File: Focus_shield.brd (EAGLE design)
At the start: 60.5 x 54.4 mm, 61 parts, among them U1 ARDUINO_SHIELDNOHOLES

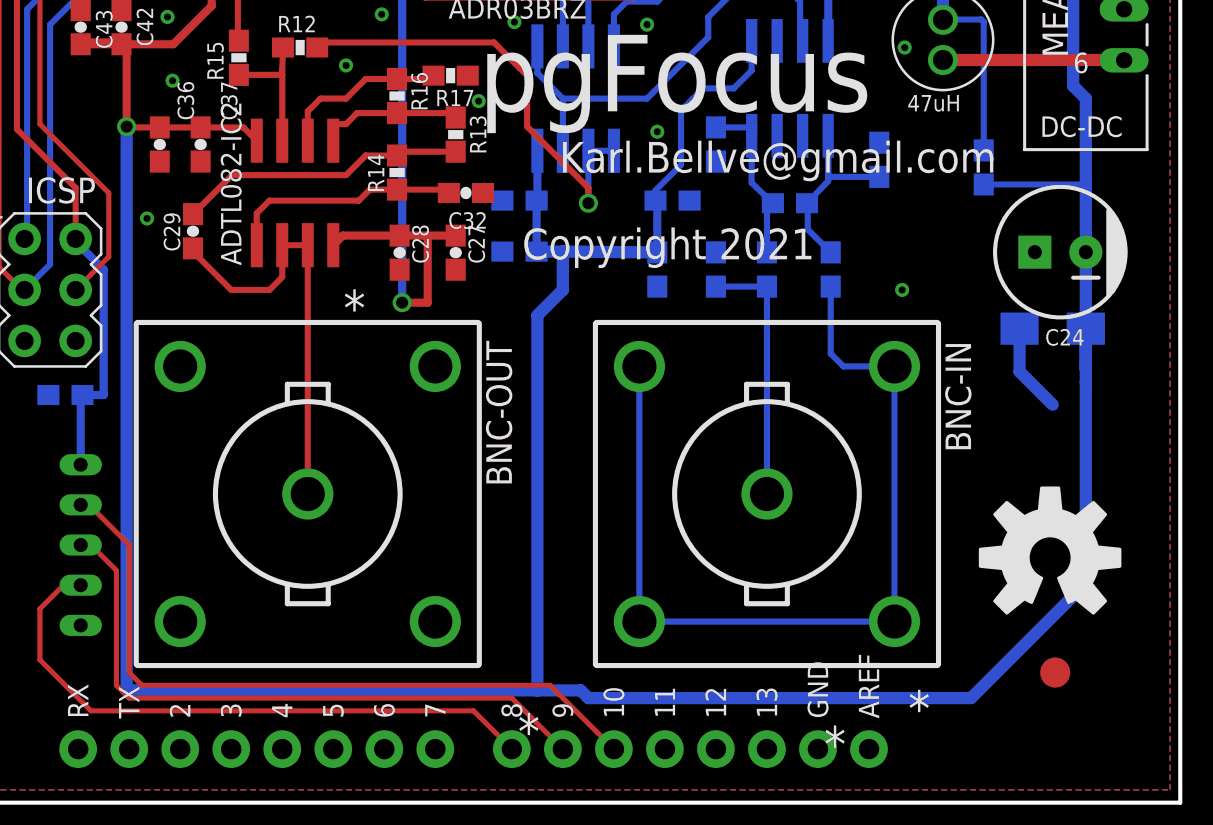
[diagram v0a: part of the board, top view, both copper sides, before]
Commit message: switch type of BNC users, and added a link to BOM spreadsheet
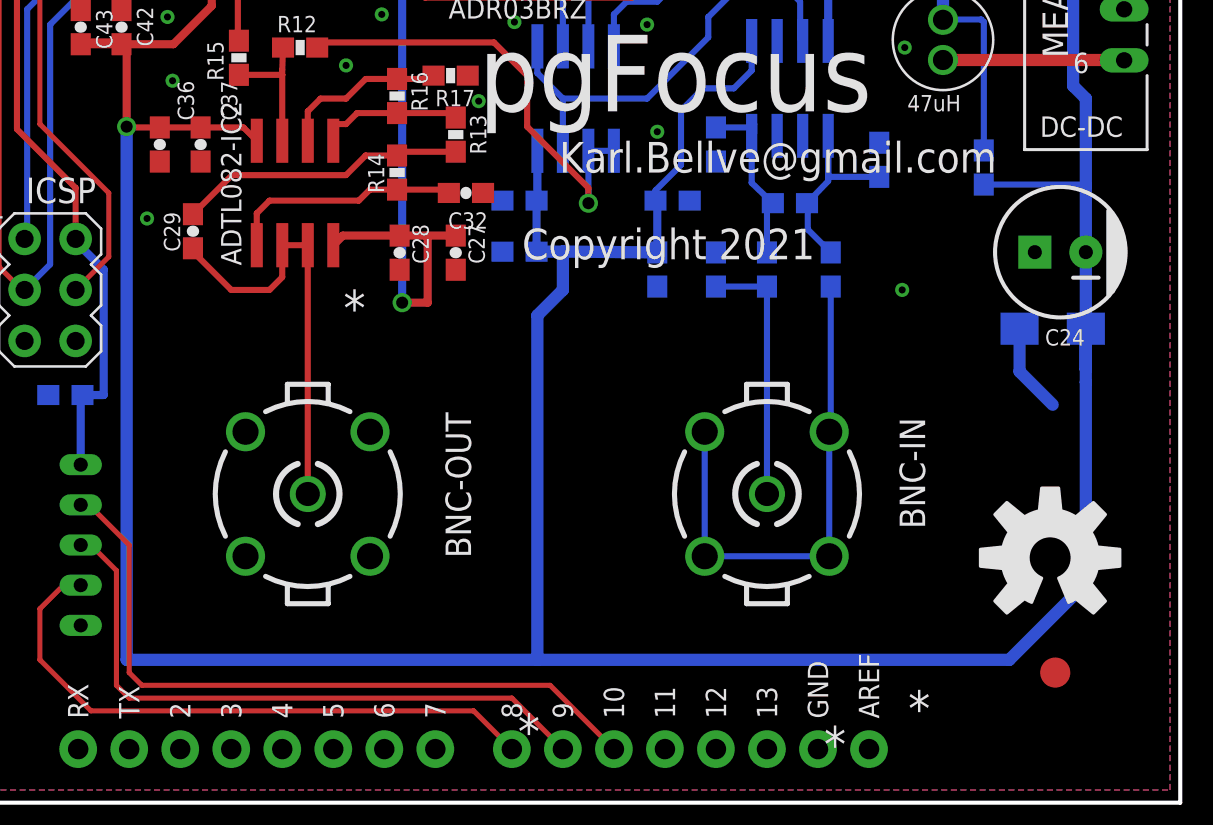
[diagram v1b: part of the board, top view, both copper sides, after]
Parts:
- BNC-IN, BNC-OUT: value B35N57 -> BN35N61; device con-coax:B35N57 -> con-coax:B35N61
- renumbered U$1 to AD5331
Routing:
- net N$13: track 44.9 -> 26.0 mm
- net -12V: track 190.1 -> 186.1 mm

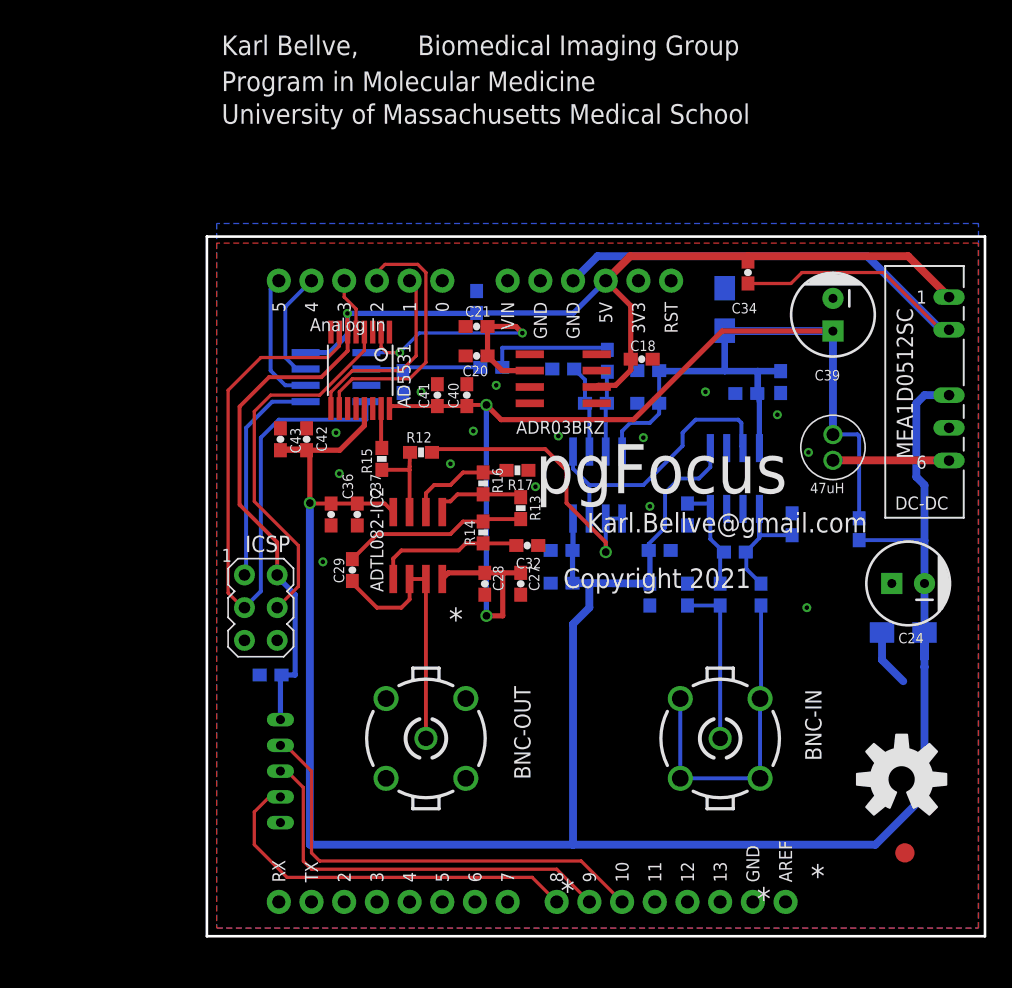
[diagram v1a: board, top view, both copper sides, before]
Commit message: moved +-12V DC power supply to other side of board to prevent shorting on Arduion USB connector. Still working on the design...not validated yet!
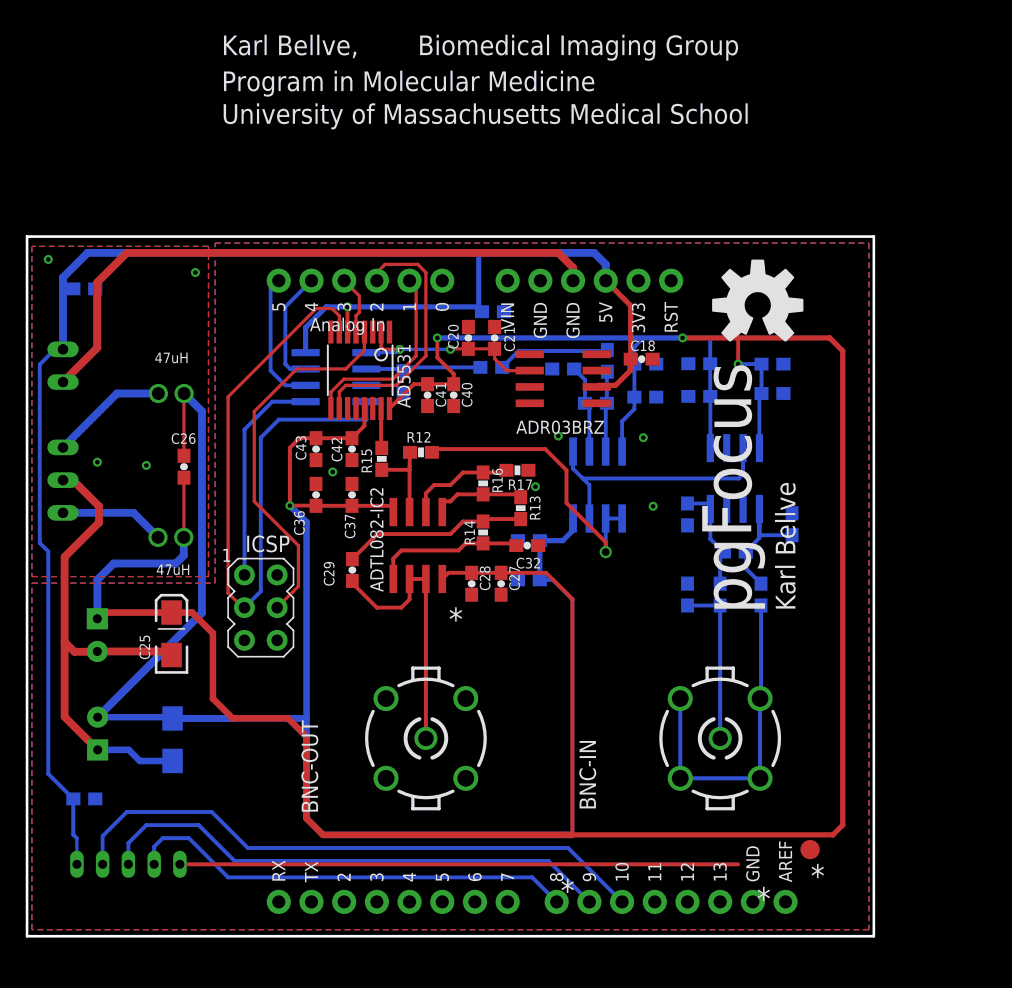
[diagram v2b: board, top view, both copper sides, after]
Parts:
- removed L3: 47uH, BIG:11R473C
- added L1, L2: 47uH, BIG:11R473C
- moved MEA1D0512SC 69.0 mm to (0.38, 44.8), flipped to the bottom
- moved C24 64.0 mm to (3.07, 21.3), flipped to the bottom, turned to 270 degrees
- moved C39 62.3 mm to (3.05, 29.0), flipped to the bottom, turned to 90 degrees
- moved C38 57.4 mm to (8.89, 20.9), turned to 270 degrees
- moved C26 52.7 mm to (9.78, 42.1), flipped to the top, turned to 90 degrees
- moved C34 51.6 mm to (2.03, 55.9), flipped to the bottom, turned to 180 degrees
- moved C25 49.8 mm to (8.81, 29.1), flipped to the top, turned to 90 degrees
- moved U$3 38.5 mm to (54.4, 54.6)
- moved C10 17.4 mm to (2.03, 16.3), turned to 180 degrees
- moved C14 15.9 mm to (49.8, 47.5), turned to 0 degrees
- moved C15 14.8 mm to (49.8, 50.1), turned to 0 degrees
- moved SENSOR 13.9 mm to (5.46, 11.2), turned to 90 degrees
- moved JP1 7.37 mm to (58.4, 12.3)
- moved C42 3.61 mm to (22.8, 43.4), turned to 90 degrees
- moved C43 2.87 mm to (20.0, 43.4), turned to 90 degrees
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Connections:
- new net N$8: L1.P$2, MEA1D0512SC.4
- new net VCC: ICSP.2
- net +12V: now also L2.P$2; no longer L3.P$2
- net +5V: no longer ICSP.2
- net -12V: now also L1.P$1; no longer MEA1D0512SC.4
- net N$6: now also L2.P$1; no longer L3.P$1
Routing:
- net +12V: track 117.7 -> 220.8 mm, vias 2 -> 3
- net GND: track 4.47 -> 83.0 mm, vias 15 -> 5
- net -12V: track 186.1 -> 234.1 mm
- net +5V: track 107.8 -> 128.6 mm
- net TSL1401R_AO: track 35.3 -> 46.2 mm
- net N$8: track 0.00 -> 9.14 mm
- net TSL1401R_CLK: track 31.6 -> 40.5 mm
- net 2.5V_REFIN: track 24.5 -> 16.6 mm
- net DCGND: track 50.2 -> 56.5 mm, vias 0 -> 4
- net TSL1401R_SI: track 30.4 -> 35.0 mm
- net AD8221: track 22.4 -> 20.3 mm
- net SCK: track 52.6 -> 53.9 mm
- net N$5: track 9.79 -> 8.73 mm
- net N$6: track 9.02 -> 8.17 mm
- added copper zone on layer 1, net DCGND
- added copper zone on layer 16, net DCGND
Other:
- board size 60.5 x 54.4 mm -> 65.8 x 54.4 mm
- board text added: "Karl Bellve"
- board text removed: "Copyright 2021"
- board text removed: "Karl.Bellve@gmail.com"

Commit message: Reworked traces. Moved power lines to the bottom. Not validated yet!
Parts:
- removed U$3: OSHW-LOGOL, SparkFun:OSHW-LOGO-L
- added +12V-PAD, -12V, GND-PAD: PTR1TP20R, testpad:TP20R
- added JP2: FIDUCIAL1.5X3, SparkFun:FIDUCIAL-1.5X3
- moved C6 19.9 mm to (53.6, 52.4), turned to 90 degrees
- moved AD7894-10 14.7 mm to (36.2, 47.4), flipped to the top, turned to 270 degrees
- moved C4 14.1 mm to (40.9, 49.5), flipped to the top, turned to 90 degrees
- moved C15 12.0 mm to (59.4, 42.9), turned to 270 degrees
- moved R8 10.3 mm to (48.7, 45.6), flipped to the top, turned to 270 degrees
- moved R10 8.98 mm to (56.8, 27.8), flipped to the top, turned to 90 degrees
- moved C19 8.88 mm to (56.5, 33.9), flipped to the top, turned to 180 degrees
- moved C7 8.82 mm to (46.5, 41.3), turned to 90 degrees
- moved C14 8.70 mm to (57.2, 42.9), turned to 270 degrees
- moved C23 8.69 mm to (49.2, 33.9), flipped to the top, turned to 180 degrees
- moved C10 8.52 mm to (10.4, 14.7), flipped to the top, turned to 0 degrees
- moved R24 8.42 mm to (40.9, 45.5), flipped to the top, turned to 90 degrees
- moved C12 8.36 mm to (44.5, 33.5), turned to 90 degrees
- moved C41 8.21 mm to (36.3, 44.6), flipped to the bottom, turned to 270 degrees
- moved R17 6.50 mm to (38.2, 35.8), turned to 90 degrees
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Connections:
- net +12V: now also +12V-PAD.TP
- net -12V: now also -12V.TP
- net GND: now also GND-PAD.TP
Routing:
- net GND: track 83.0 -> 39.6 mm, vias 5 -> 9
- net +5V: track 128.6 -> 155.9 mm, vias 1 -> 3
- net -12V: track 234.1 -> 210.8 mm, vias 1 -> 5
- net ADC_CONVST: track 9.05 -> 27.0 mm
- net +12V: track 220.8 -> 203.0 mm, vias 3 -> 7
- net ADC_BUSY: track 10.4 -> 27.2 mm
- net SCK: track 53.9 -> 38.8 mm, vias 0 -> 3
- net MISO: track 16.9 -> 29.3 mm
- net AD8221: track 20.3 -> 13.4 mm
- net N$5: track 8.73 -> 2.08 mm
- net DAC_SS: track 4.58 -> 10.8 mm
- net TSL1401R_AO: track 46.2 -> 40.2 mm
- net BNCVIN: track 22.7 -> 17.2 mm, vias 1 -> 0
- net N$1: track 8.46 -> 12.9 mm
- net TSL1401R_SI: track 35.0 -> 39.2 mm
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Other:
- board text added: "+12V"
- board text added: "-12V"
- board text added: "GND"

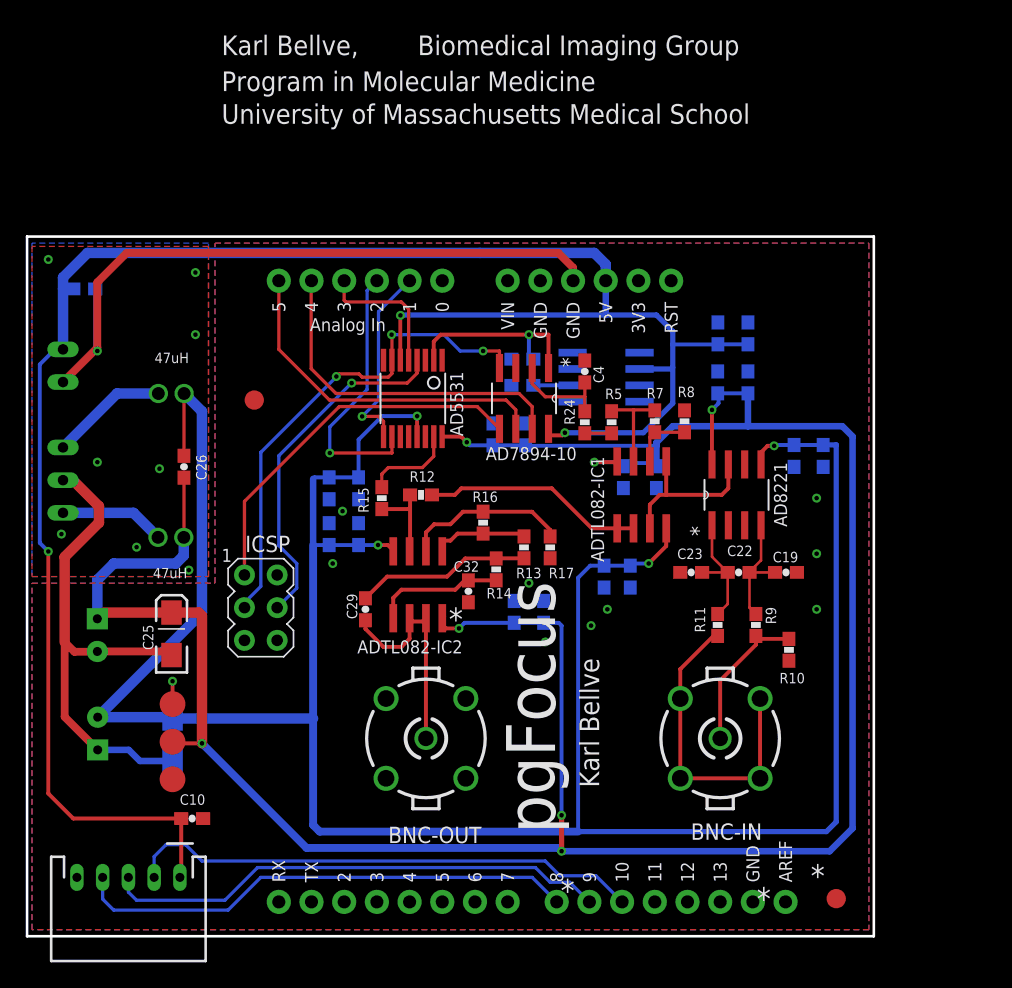
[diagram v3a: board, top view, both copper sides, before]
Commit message: Added solder jumnpers to adjust voltage range and gain settings of the ADC and DAC chips. Still untested!
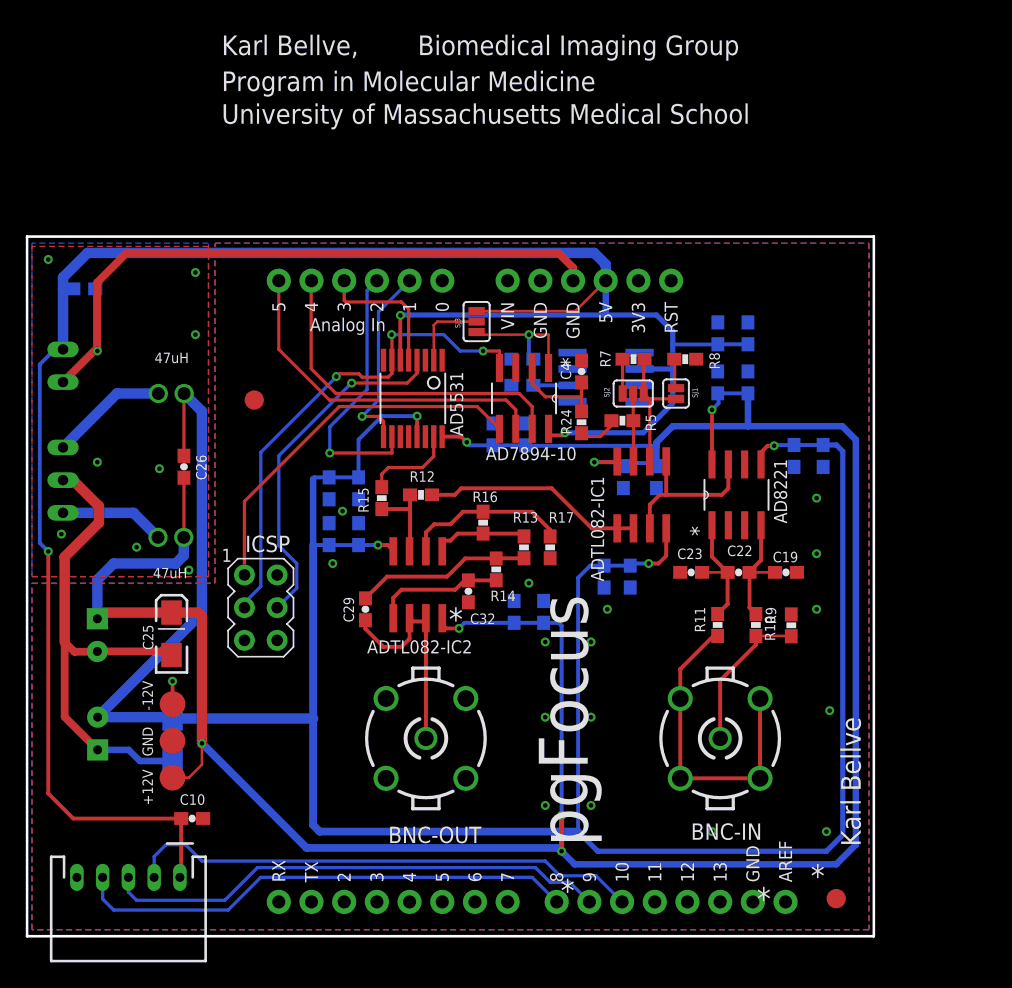
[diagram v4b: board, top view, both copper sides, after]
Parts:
- added SJ1: SOLDERJUMPERNC, SparkFun-Passives:SJ_2S
- added SJ2, SJ3: (no value), SparkFun-Passives:SJ_3_PASTE2&3
- AD5331: value AD5531 -> AD5331
- moved R7 5.10 mm to (44.7, 50.4), turned to 0 degrees
- moved R8 4.83 mm to (48.7, 50.4), turned to 180 degrees
- moved GND-PAD 2.98 mm to (8.89, 20.8)
- moved +12V-PAD 2.79 mm to (8.89, 17.9)
- moved R10 1.91 mm to (57.0, 29.7), turned to 270 degrees
- moved R5 0.85 mm to (43.8, 45.6), turned to 180 degrees
- moved C4 0.25 mm to (40.7, 49.5)
- moved R24 0.25 mm to (40.7, 45.5)
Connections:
- new net N$10: R8.2, SJ1.1
- new net N$9: R7.1, SJ2.3
- new net REFIN: AD5331.REFIN, SJ3.2
- net +5V: now also SJ3.1
- net 2.5V_REFIN: now also SJ3.3; no longer AD5331.REFIN
- net AD7894-10: now also SJ2.2; no longer R7.1
- net N$18: now also SJ1.2, SJ2.1; no longer R8.2
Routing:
- net +5V: track 155.9 -> 166.9 mm
- net N$18: track 4.73 -> 11.6 mm
- net REFIN: track 0.00 -> 6.16 mm
- net 2.5V_REFIN: track 20.3 -> 15.4 mm
- net +12V: track 203.0 -> 207.0 mm
- net -12V: track 210.8 -> 213.8 mm
- net N$9: track 0.00 -> 2.67 mm
- net N$10: track 0.00 -> 2.31 mm
- net AD7894-10: track 7.42 -> 5.28 mm
- net N$5: track 2.08 -> 3.16 mm
- net GND: vias 9 -> 16
